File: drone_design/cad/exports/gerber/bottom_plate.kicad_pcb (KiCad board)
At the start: 2 copper layers, 120 x 120 mm, 124 parts

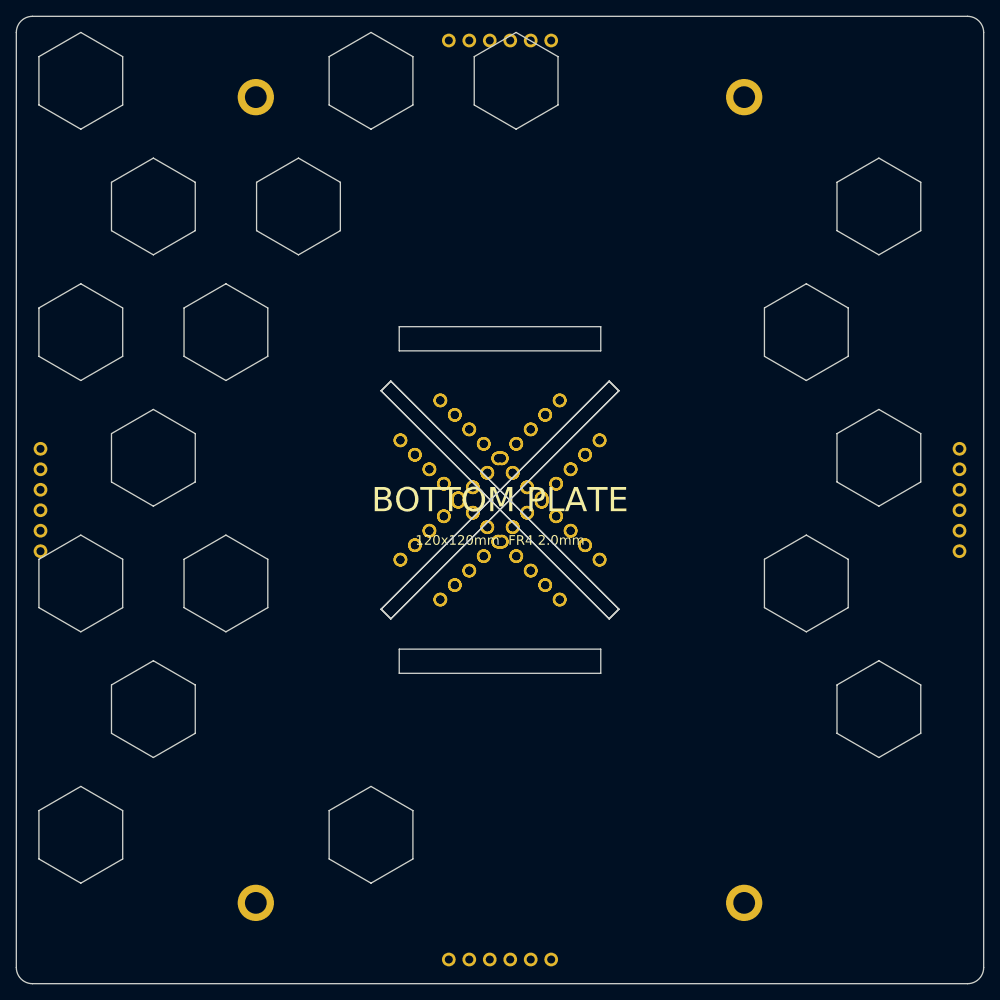
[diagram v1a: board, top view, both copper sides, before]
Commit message: feat: modular two-section arms and nose boom with adjustable length
Arms split into inner (tab) + outer (motor) sections with 40mm
I-beam overlap zone. 4x M2 slider holes at 10mm pitch allow
adjustable motor distance. Same pattern for nose boom: root (190mm)
+ tip (230mm) sections with web/collar interlock.

- arm.py: make_arm_inner(), make_arm_outer(), make_arm() (compat)
- nose_boom.py: make_boom_root(), make_boom_tip(), make_nose_boom()
- export_stl.py: add arm_inner, arm_outer, boom_root, boom_tip
  as individual exportable parts with COMPONENT_CATALOG metadata
- Refactored drone_3d_model.py with assembly_constants module
- All 23 individual parts + 49 assembly parts export cleanly
- Removed obsolete drone_3d_model.scad
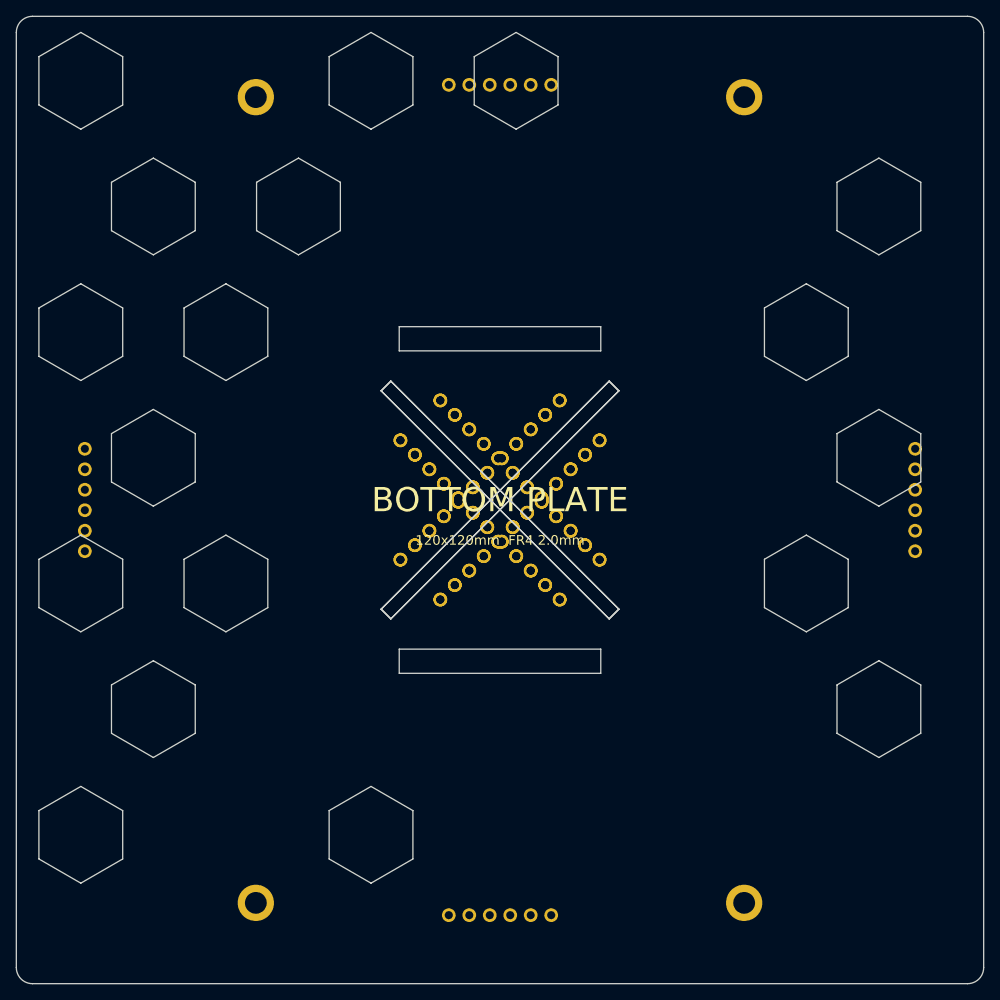
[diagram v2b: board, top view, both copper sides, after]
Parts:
- removed the ? at (1.58, -3.37) (x2)
- removed the ? at (12.4, -7.40) (x2)
- removed the ? at (57.0, -6.35)
- removed the ? at (57.0, -3.81)
- removed the ? at (57.0, -1.27)
- removed the ? at (57.0, 1.27)
- removed the ? at (57.0, 3.81)
- removed the ? at (57.0, 6.35)
- removed the ? at (6.35, 57.0)
- removed the ? at (3.81, 57.0)
- removed the ? at (1.27, 57.0)
- removed the ? at (3.37, -1.58) (x2)
- removed the ? at (-1.27, 57.0)
- removed the ? at (-3.81, 57.0)
- removed the ? at (-6.35, 57.0)
- removed the ? at (-57.0, 6.35)
- removed the ? at (-57.0, 3.81)
- removed the ? at (-57.0, 1.27)
- removed the ? at (-57.0, -1.27)
- removed the ? at (-57.0, -3.81)
- removed the ? at (-57.0, -6.35)
- removed the ? at (-6.35, -57.0)
- removed the ? at (5.17, 0.22) (x2)
- removed the ? at (-3.81, -57.0)
- removed the ? at (-1.27, -57.0)
- removed the ? at (1.27, -57.0)
- removed the ? at (3.81, -57.0)
- removed the ? at (6.35, -57.0)
- removed the ? at (6.96, 2.02) (x2)
- removed the ? at (8.76, 3.81) (x2)
- removed the ? at (10.6, 5.61) (x2)
- removed the ? at (12.4, 7.40) (x2)
- removed the ? at (-12.4, -7.40) (x2)
- removed the ? at (-10.6, -5.61) (x2)
- removed the ? at (-8.76, -3.81) (x2)
- removed the ? at (-6.96, -2.02) (x2)
- removed the ? at (-5.17, -0.22) (x2)
- removed the ? at (-3.37, 1.58) (x2)
- removed the ? at (-1.58, 3.37) (x2)
- removed the ? at (0.22, 5.17) (x2)
- removed the ? at (2.02, 6.96) (x2)
- removed the ? at (3.81, 8.76) (x2)
- removed the ? at (5.61, 10.6) (x2)
- removed the ? at (7.40, 12.4) (x2)
- removed the ? at (10.6, -5.61) (x2)
- removed the ? at (8.76, -3.81) (x2)
- removed the ? at (6.96, -2.02) (x2)
- removed the ? at (5.17, -0.22) (x2)
- removed the ? at (3.37, 1.58) (x2)
- removed the ? at (1.58, 3.37) (x2)
- removed the ? at (-0.22, 5.17) (x2)
- removed the ? at (-2.02, 6.96) (x2)
- removed the ? at (-3.81, 8.76) (x2)
- removed the ? at (-5.61, 10.6) (x2)
- removed the ? at (-7.40, 12.4) (x2)
- removed the ? at (7.40, -12.4) (x2)
- removed the ? at (5.61, -10.6) (x2)
- removed the ? at (3.81, -8.76) (x2)
- removed the ? at (2.02, -6.96) (x2)
- removed the ? at (0.22, -5.17) (x2)
- removed the ? at (-1.58, -3.37) (x2)
- removed the ? at (-3.37, -1.58) (x2)
- removed the ? at (-5.17, 0.22) (x2)
- removed the ? at (-6.96, 2.02) (x2)
- removed the ? at (-7.40, -12.4) (x2)
- removed the ? at (-8.76, 3.81) (x2)
- removed the ? at (-10.6, 5.61) (x2)
- removed the ? at (-12.4, 7.40) (x2)
- removed the ? at (-5.61, -10.6) (x2)
- removed the ? at (-3.81, -8.76) (x2)
- removed the ? at (-0.22, -5.17) (x2)
- removed the ? at (-2.02, -6.96) (x2)
- added ? (x2): , MountingHole:MountingHole_1.0mm, F.Cu at (1.58, -3.37)
- added ? (x2): , MountingHole:MountingHole_1.0mm, F.Cu at (12.4, -7.40)
- added ?: , MountingHole:MountingHole_1.0mm, F.Cu at (51.5, -6.35)
- added ?: , MountingHole:MountingHole_1.0mm, F.Cu at (51.5, -3.81)
- added ?: , MountingHole:MountingHole_1.0mm, F.Cu at (51.5, -1.27)
- added ?: , MountingHole:MountingHole_1.0mm, F.Cu at (51.5, 1.27)
- added ?: , MountingHole:MountingHole_1.0mm, F.Cu at (51.5, 3.81)
- added ?: , MountingHole:MountingHole_1.0mm, F.Cu at (51.5, 6.35)
- added ?: , MountingHole:MountingHole_1.0mm, F.Cu at (6.35, 51.5)
- added ?: , MountingHole:MountingHole_1.0mm, F.Cu at (3.81, 51.5)
- added ?: , MountingHole:MountingHole_1.0mm, F.Cu at (1.27, 51.5)
- added ? (x2): , MountingHole:MountingHole_1.0mm, F.Cu at (3.37, -1.58)
- added ?: , MountingHole:MountingHole_1.0mm, F.Cu at (-1.27, 51.5)
- added ?: , MountingHole:MountingHole_1.0mm, F.Cu at (-3.81, 51.5)
- added ?: , MountingHole:MountingHole_1.0mm, F.Cu at (-6.35, 51.5)
- added ?: , MountingHole:MountingHole_1.0mm, F.Cu at (-51.5, 6.35)
- added ?: , MountingHole:MountingHole_1.0mm, F.Cu at (-51.5, 3.81)
- added ?: , MountingHole:MountingHole_1.0mm, F.Cu at (-51.5, 1.27)
- added ?: , MountingHole:MountingHole_1.0mm, F.Cu at (-51.5, -1.27)
- added ?: , MountingHole:MountingHole_1.0mm, F.Cu at (-51.5, -3.81)
- added ?: , MountingHole:MountingHole_1.0mm, F.Cu at (-51.5, -6.35)
- added ?: , MountingHole:MountingHole_1.0mm, F.Cu at (-6.35, -51.5)
- added ? (x2): , MountingHole:MountingHole_1.0mm, F.Cu at (5.17, 0.22)
- added ?: , MountingHole:MountingHole_1.0mm, F.Cu at (-3.81, -51.5)
- added ?: , MountingHole:MountingHole_1.0mm, F.Cu at (-1.27, -51.5)
- added ?: , MountingHole:MountingHole_1.0mm, F.Cu at (1.27, -51.5)
- added ?: , MountingHole:MountingHole_1.0mm, F.Cu at (3.81, -51.5)
- added ?: , MountingHole:MountingHole_1.0mm, F.Cu at (6.35, -51.5)
- added ? (x2): , MountingHole:MountingHole_1.0mm, F.Cu at (6.96, 2.02)
- added ? (x2): , MountingHole:MountingHole_1.0mm, F.Cu at (8.76, 3.81)
- added ? (x2): , MountingHole:MountingHole_1.0mm, F.Cu at (10.6, 5.61)
- added ? (x2): , MountingHole:MountingHole_1.0mm, F.Cu at (12.4, 7.40)
- added ? (x2): , MountingHole:MountingHole_1.0mm, F.Cu at (-12.4, -7.40)
- added ? (x2): , MountingHole:MountingHole_1.0mm, F.Cu at (-10.6, -5.61)
- added ? (x2): , MountingHole:MountingHole_1.0mm, F.Cu at (-8.76, -3.81)
- added ? (x2): , MountingHole:MountingHole_1.0mm, F.Cu at (-6.96, -2.02)
- added ? (x2): , MountingHole:MountingHole_1.0mm, F.Cu at (-5.17, -0.22)
- added ? (x2): , MountingHole:MountingHole_1.0mm, F.Cu at (-3.37, 1.58)
- added ? (x2): , MountingHole:MountingHole_1.0mm, F.Cu at (-1.58, 3.37)
- added ? (x2): , MountingHole:MountingHole_1.0mm, F.Cu at (0.22, 5.17)
- added ? (x2): , MountingHole:MountingHole_1.0mm, F.Cu at (2.02, 6.96)
- added ? (x2): , MountingHole:MountingHole_1.0mm, F.Cu at (3.81, 8.76)
- added ? (x2): , MountingHole:MountingHole_1.0mm, F.Cu at (5.61, 10.6)
- added ? (x2): , MountingHole:MountingHole_1.0mm, F.Cu at (7.40, 12.4)
- added ? (x2): , MountingHole:MountingHole_1.0mm, F.Cu at (10.6, -5.61)
- added ? (x2): , MountingHole:MountingHole_1.0mm, F.Cu at (8.76, -3.81)
- added ? (x2): , MountingHole:MountingHole_1.0mm, F.Cu at (6.96, -2.02)
- added ? (x2): , MountingHole:MountingHole_1.0mm, F.Cu at (5.17, -0.22)
- added ? (x2): , MountingHole:MountingHole_1.0mm, F.Cu at (3.37, 1.58)
- added ? (x2): , MountingHole:MountingHole_1.0mm, F.Cu at (1.58, 3.37)
- added ? (x2): , MountingHole:MountingHole_1.0mm, F.Cu at (-0.22, 5.17)
- added ? (x2): , MountingHole:MountingHole_1.0mm, F.Cu at (-2.02, 6.96)
- added ? (x2): , MountingHole:MountingHole_1.0mm, F.Cu at (-3.81, 8.76)
- added ? (x2): , MountingHole:MountingHole_1.0mm, F.Cu at (-5.61, 10.6)
- added ? (x2): , MountingHole:MountingHole_1.0mm, F.Cu at (-7.40, 12.4)
- added ? (x2): , MountingHole:MountingHole_1.0mm, F.Cu at (7.40, -12.4)
- added ? (x2): , MountingHole:MountingHole_1.0mm, F.Cu at (5.61, -10.6)
- added ? (x2): , MountingHole:MountingHole_1.0mm, F.Cu at (3.81, -8.76)
- added ? (x2): , MountingHole:MountingHole_1.0mm, F.Cu at (2.02, -6.96)
- added ? (x2): , MountingHole:MountingHole_1.0mm, F.Cu at (0.22, -5.17)
- added ? (x2): , MountingHole:MountingHole_1.0mm, F.Cu at (-1.58, -3.37)
- added ? (x2): , MountingHole:MountingHole_1.0mm, F.Cu at (-3.37, -1.58)
- added ? (x2): , MountingHole:MountingHole_1.0mm, F.Cu at (-5.17, 0.22)
- added ? (x2): , MountingHole:MountingHole_1.0mm, F.Cu at (-6.96, 2.02)
- added ? (x2): , MountingHole:MountingHole_1.0mm, F.Cu at (-7.40, -12.4)
- added ? (x2): , MountingHole:MountingHole_1.0mm, F.Cu at (-8.76, 3.81)
- added ? (x2): , MountingHole:MountingHole_1.0mm, F.Cu at (-10.6, 5.61)
- added ? (x2): , MountingHole:MountingHole_1.0mm, F.Cu at (-12.4, 7.40)
- added ? (x2): , MountingHole:MountingHole_1.0mm, F.Cu at (-5.61, -10.6)
- added ? (x2): , MountingHole:MountingHole_1.0mm, F.Cu at (-3.81, -8.76)
- added ? (x2): , MountingHole:MountingHole_1.0mm, F.Cu at (-0.22, -5.17)
- added ? (x2): , MountingHole:MountingHole_1.0mm, F.Cu at (-2.02, -6.96)
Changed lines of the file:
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@@
   )
   (footprint "MountingHole:MountingHole_1.0mm" (layer "F.Cu")
-    (at 57.0000 -6.3500)
+    (at 51.5000 -6.3500)
     (pad "" thru_hole circle (at 0 0) (size 1.70 1.70) (drill 1.00)
       (layers "*.Cu" "*.Mask")
@@
   )
   (footprint "MountingHole:MountingHole_1.0mm" (layer "F.Cu")
-    (at 57.0000 -3.8100)
+    (at 51.5000 -3.8100)
     (pad "" thru_hole circle (at 0 0) (size 1.70 1.70) (drill 1.00)
       (layers "*.Cu" "*.Mask")
@@
   )
   (footprint "MountingHole:MountingHole_1.0mm" (layer "F.Cu")
-    (at 57.0000 -1.2700)
+    (at 51.5000 -1.2700)
     (pad "" thru_hole circle (at 0 0) (size 1.70 1.70) (drill 1.00)
       (layers "*.Cu" "*.Mask")
@@
   )
   (footprint "MountingHole:MountingHole_1.0mm" (layer "F.Cu")
-    (at 57.0000 1.2700)
+    (at 51.5000 1.2700)
     (pad "" thru_hole circle (at 0 0) (size 1.70 1.70) (drill 1.00)
       (layers "*.Cu" "*.Mask")
@@
   )
   (footprint "MountingHole:MountingHole_1.0mm" (layer "F.Cu")
-    (at 57.0000 3.8100)
+    (at 51.5000 3.8100)
     (pad "" thru_hole circle (at 0 0) (size 1.70 1.70) (drill 1.00)
       (layers "*.Cu" "*.Mask")
@@
   )
   (footprint "MountingHole:MountingHole_1.0mm" (layer "F.Cu")
-    (at 57.0000 6.3500)
+    (at 51.5000 6.3500)
     (pad "" thru_hole circle (at 0 0) (size 1.70 1.70) (drill 1.00)
       (layers "*.Cu" "*.Mask")
@@
   )
   (footprint "MountingHole:MountingHole_1.0mm" (layer "F.Cu")
-    (at 6.3500 57.0000)
+    (at 6.3500 51.5000)
     (pad "" thru_hole circle (at 0 0) (size 1.70 1.70) (drill 1.00)
       (layers "*.Cu" "*.Mask")
@@
   )
   (footprint "MountingHole:MountingHole_1.0mm" (layer "F.Cu")
-    (at 3.8100 57.0000)
+    (at 3.8100 51.5000)
     (pad "" thru_hole circle (at 0 0) (size 1.70 1.70) (drill 1.00)
       (layers "*.Cu" "*.Mask")
@@
   )
   (footprint "MountingHole:MountingHole_1.0mm" (layer "F.Cu")
-    (at 1.2700 57.0000)
+    (at 1.2700 51.5000)
     (pad "" thru_hole circle (at 0 0) (size 1.70 1.70) (drill 1.00)
       (layers "*.Cu" "*.Mask")
@@
   )
   (footprint "MountingHole:MountingHole_1.0mm" (layer "F.Cu")
-    (at -1.2700 57.0000)
+    (at -1.2700 51.5000)
     (pad "" thru_hole circle (at 0 0) (size 1.70 1.70) (drill 1.00)
       (layers "*.Cu" "*.Mask")
@@
   )
   (footprint "MountingHole:MountingHole_1.0mm" (layer "F.Cu")
-    (at -3.8100 57.0000)
+    (at -3.8100 51.5000)
     (pad "" thru_hole circle (at 0 0) (size 1.70 1.70) (drill 1.00)
       (layers "*.Cu" "*.Mask")
@@
   )
   (footprint "MountingHole:MountingHole_1.0mm" (layer "F.Cu")
-    (at -6.3500 57.0000)
+    (at -6.3500 51.5000)
     (pad "" thru_hole circle (at 0 0) (size 1.70 1.70) (drill 1.00)
       (layers "*.Cu" "*.Mask")
@@
   )
   (footprint "MountingHole:MountingHole_1.0mm" (layer "F.Cu")
-    (at -57.0000 6.3500)
+    (at -51.5000 6.3500)
     (pad "" thru_hole circle (at 0 0) (size 1.70 1.70) (drill 1.00)
       (layers "*.Cu" "*.Mask")
@@
   )
   (footprint "MountingHole:MountingHole_1.0mm" (layer "F.Cu")
-    (at -57.0000 3.8100)
+    (at -51.5000 3.8100)
     (pad "" thru_hole circle (at 0 0) (size 1.70 1.70) (drill 1.00)
       (layers "*.Cu" "*.Mask")
@@
   )
   (footprint "MountingHole:MountingHole_1.0mm" (layer "F.Cu")
-    (at -57.0000 1.2700)
+    (at -51.5000 1.2700)
     (pad "" thru_hole circle (at 0 0) (size 1.70 1.70) (drill 1.00)
       (layers "*.Cu" "*.Mask")
@@
   )
   (footprint "MountingHole:MountingHole_1.0mm" (layer "F.Cu")
-    (at -57.0000 -1.2700)
+    (at -51.5000 -1.2700)
     (pad "" thru_hole circle (at 0 0) (size 1.70 1.70) (drill 1.00)
       (layers "*.Cu" "*.Mask")
@@
   )
   (footprint "MountingHole:MountingHole_1.0mm" (layer "F.Cu")
-    (at -57.0000 -3.8100)
+    (at -51.5000 -3.8100)
     (pad "" thru_hole circle (at 0 0) (size 1.70 1.70) (drill 1.00)
       (layers "*.Cu" "*.Mask")
@@
   )
   (footprint "MountingHole:MountingHole_1.0mm" (layer "F.Cu")
-    (at -57.0000 -6.3500)
+    (at -51.5000 -6.3500)
     (pad "" thru_hole circle (at 0 0) (size 1.70 1.70) (drill 1.00)
       (layers "*.Cu" "*.Mask")
@@
   )
   (footprint "MountingHole:MountingHole_1.0mm" (layer "F.Cu")
-    (at -6.3500 -57.0000)
+    (at -6.3500 -51.5000)
     (pad "" thru_hole circle (at 0 0) (size 1.70 1.70) (drill 1.00)
       (layers "*.Cu" "*.Mask")
@@
   )
   (footprint "MountingHole:MountingHole_1.0mm" (layer "F.Cu")
-    (at -3.8100 -57.0000)
+    (at -3.8100 -51.5000)
     (pad "" thru_hole circle (at 0 0) (size 1.70 1.70) (drill 1.00)
       (layers "*.Cu" "*.Mask")
@@
   )
   (footprint "MountingHole:MountingHole_1.0mm" (layer "F.Cu")
-    (at -1.2700 -57.0000)
+    (at -1.2700 -51.5000)
     (pad "" thru_hole circle (at 0 0) (size 1.70 1.70) (drill 1.00)
       (layers "*.Cu" "*.Mask")
@@
   )
   (footprint "MountingHole:MountingHole_1.0mm" (layer "F.Cu")
-    (at 1.2700 -57.0000)
+    (at 1.2700 -51.5000)
     (pad "" thru_hole circle (at 0 0) (size 1.70 1.70) (drill 1.00)
       (layers "*.Cu" "*.Mask")
@@
   )
   (footprint "MountingHole:MountingHole_1.0mm" (layer "F.Cu")
-    (at 3.8100 -57.0000)
+    (at 3.8100 -51.5000)
     (pad "" thru_hole circle (at 0 0) (size 1.70 1.70) (drill 1.00)
       (layers "*.Cu" "*.Mask")
@@
   )
   (footprint "MountingHole:MountingHole_1.0mm" (layer "F.Cu")
-    (at 6.3500 -57.0000)
+    (at 6.3500 -51.5000)
     (pad "" thru_hole circle (at 0 0) (size 1.70 1.70) (drill 1.00)
       (layers "*.Cu" "*.Mask")
